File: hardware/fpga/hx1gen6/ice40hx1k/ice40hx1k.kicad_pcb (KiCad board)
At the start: 2 copper layers, 96.8 x 77 mm, 58 parts, among them J1 Conn_01x20_Male, J2 Conn_01x20_Male, J3 Conn_01x20_Male, U1 LTC3406ES5, U5 AT25SF081-SSHD-X, U6 ICE40HX1K-VQ100(VQFP100), U7 AS7C34096A, X2 ASE-10MHz, X3 ASE-10MHz, X4 ASE-10MHz, X5 ASV-xxxMHz, X6 ASV-xxxMHz, X7 ASV-xxxMHz

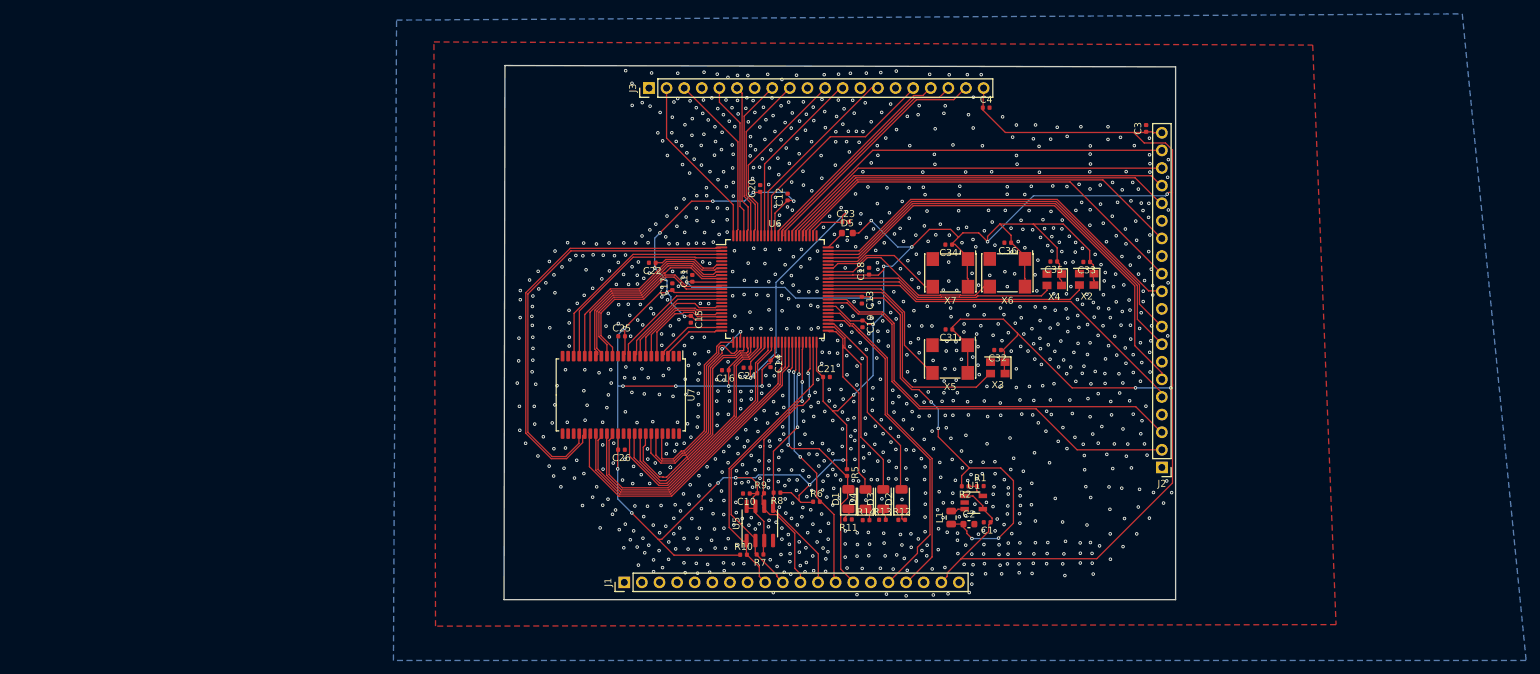
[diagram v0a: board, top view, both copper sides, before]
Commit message: preparing FSK and phase experiments: started HX1K gen6 brd
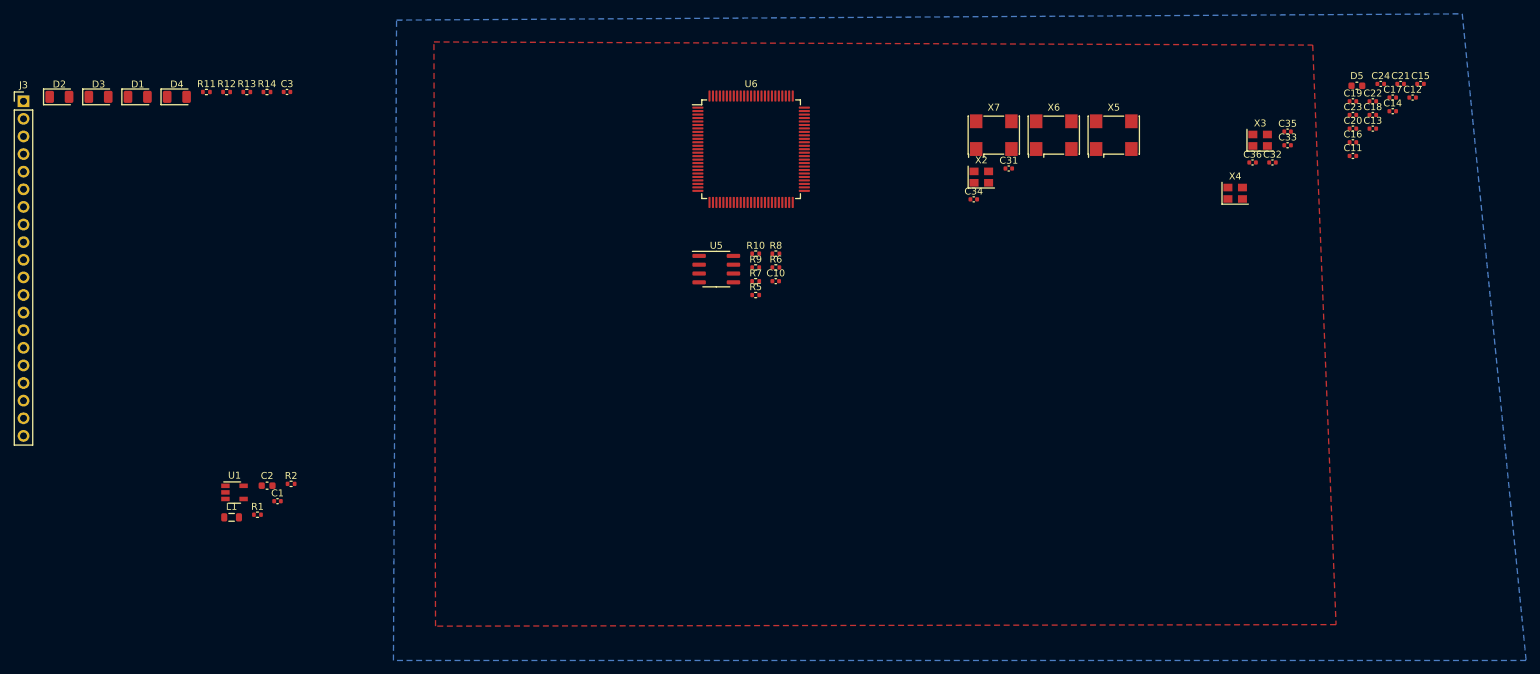
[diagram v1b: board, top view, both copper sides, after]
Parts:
- removed C25, C26: 0.1uF, Capacitor_SMD:C_0402_1005Metric
- removed C4: 1uF, Capacitor_SMD:C_0402_1005Metric
- removed J1, J2: Conn_01x20_Male, Connector_PinHeader_2.54mm:PinHeader_1x20_P2.54mm_Vertical
- removed U7: AS7C34096A, Package_SO:TSOP-II-44_10.16x18.41mm_P0.8mm
- moved D2 134.6 mm to (49.0, 78.4), turned to 0 degrees
- moved D3 127.2 mm to (54.7, 78.4), turned to 0 degrees
- moved C3 124.0 mm to (81.8, 77.7), turned to 0 degrees
- moved D1 117.8 mm to (60.3, 78.4), turned to 0 degrees
- moved R12 115.3 mm to (73.1, 77.7)
- moved D4 115.0 mm to (66.0, 78.4), turned to 0 degrees
- moved R11 111.2 mm to (70.2, 77.7), turned to 0 degrees
- moved C15 110.6 mm to (245.3, 76.6), turned to 0 degrees
- moved R13 110.5 mm to (76.0, 77.7)
- moved C17 107.4 mm to (241.3, 78.5), turned to 0 degrees
- moved U1 106.6 mm to (74.3, 135.5)
- moved C22 106.5 mm to (238.4, 79.1), turned to 0 degrees
- moved R14 106.2 mm to (79.0, 77.7)
- moved R1 104.3 mm to (77.6, 138.7)
- moved L1 103.8 mm to (73.9, 139.1), turned to 0 degrees
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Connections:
- U6 pad 1: IO1 -> IO1_1A
- U6 pad 10: IO10 -> IO10_5B
- U6 pad 12: IO12 -> IO12_6A
- U6 pad 13: IO13 -> IO13_6B
- U6 pad 15: IO15 -> IO15_7A
- U6 pad 16: IO16 -> IO16_7B
- U6 pad 18: IO18 -> IO18_8A
- U6 pad 19: IO19 -> IO19_8B
- U6 pad 2: IO2 -> IO2_1A
- U6 pad 20: IO20 -> IO20_10A
- U6 pad 21: IO21 -> IO21_10B
- U6 pad 24: IO24 -> IO24_12A
- U6 pad 25: IO25 -> IO25_12B
- U6 pad 3: IO3 -> IO3_2A
- U6 pad 4: IO4 -> IO4_2B
- U6 pad 7: IO7 -> IO7_3A
- U6 pad 8: IO8 -> IO8_3B
- U6 pad 9: IO9 -> IO9_5A
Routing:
- net +3V3: track 593.3 -> 0.00 mm, vias 27 -> 0
- net +1V2: track 141.8 -> 0.00 mm, vias 8 -> 0
- net IO71: track 67.6 -> 0.00 mm
- net IO1: track 63.1 -> 0.00 mm
- net IO72: track 62.7 -> 0.00 mm
- net IO59: track 61.6 -> 0.00 mm
- net IO2: track 61.5 -> 0.00 mm
- net IO60: track 61.0 -> 0.00 mm
- net IO73: track 60.2 -> 0.00 mm
- net IO78: track 60.2 -> 0.00 mm
- net IO83: track 58.7 -> 0.00 mm
- net IO79: track 58.6 -> 0.00 mm
- net IO80: track 57.4 -> 0.00 mm
- net IO82: track 57.2 -> 0.00 mm
- net IO81: track 57.0 -> 0.00 mm
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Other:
- board outline removed
